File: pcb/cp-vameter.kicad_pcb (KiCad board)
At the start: 2 copper layers, 100 x 100 mm, 28 parts, among them J1 Vin JST-PH2, J10 Vin Header*, J11 Vin JST-PH2, J12 Grove Ext. INA260, J13 Grove Display, J14 Grove Keypad, J15 Conn Display, J16 Conn Keypad, J2 Vin Header*, J3 Vin Barrel-Jack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

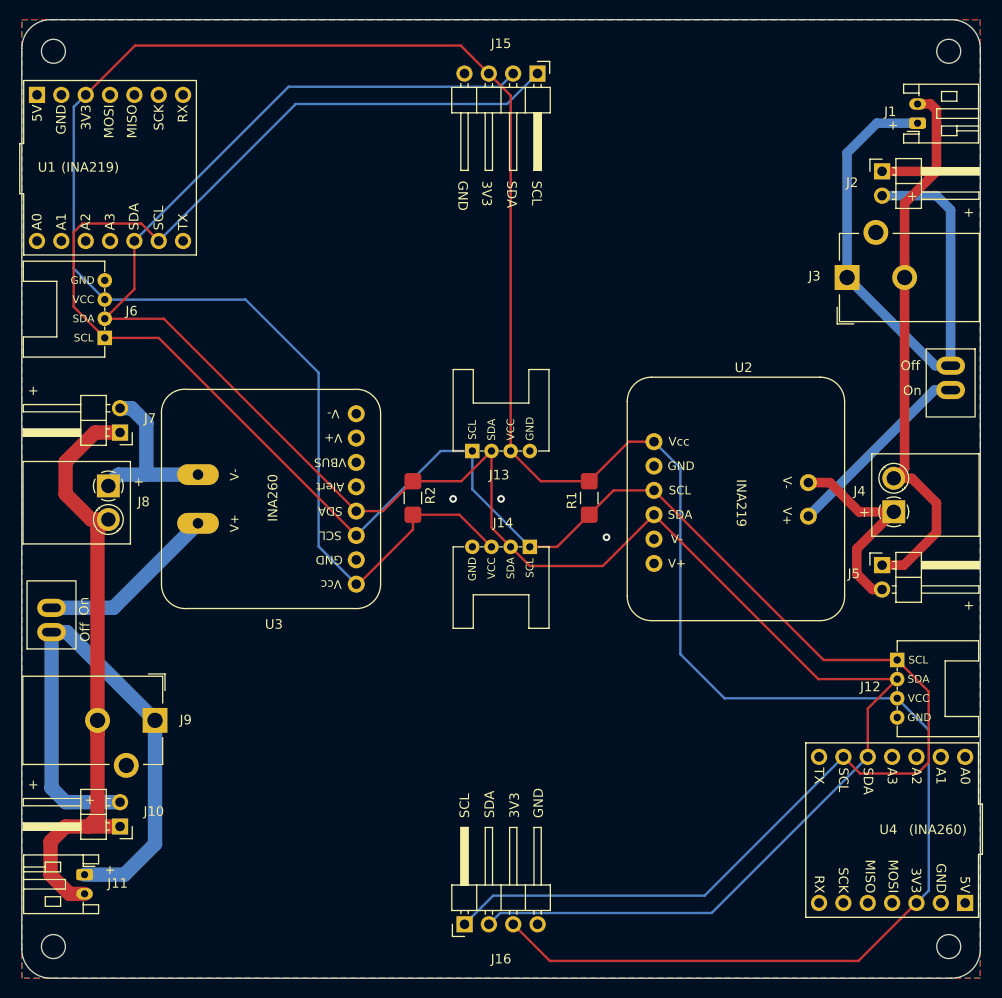
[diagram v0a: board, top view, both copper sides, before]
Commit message: replaced tht-footprint with smd-footprint for JST-connector in pcb
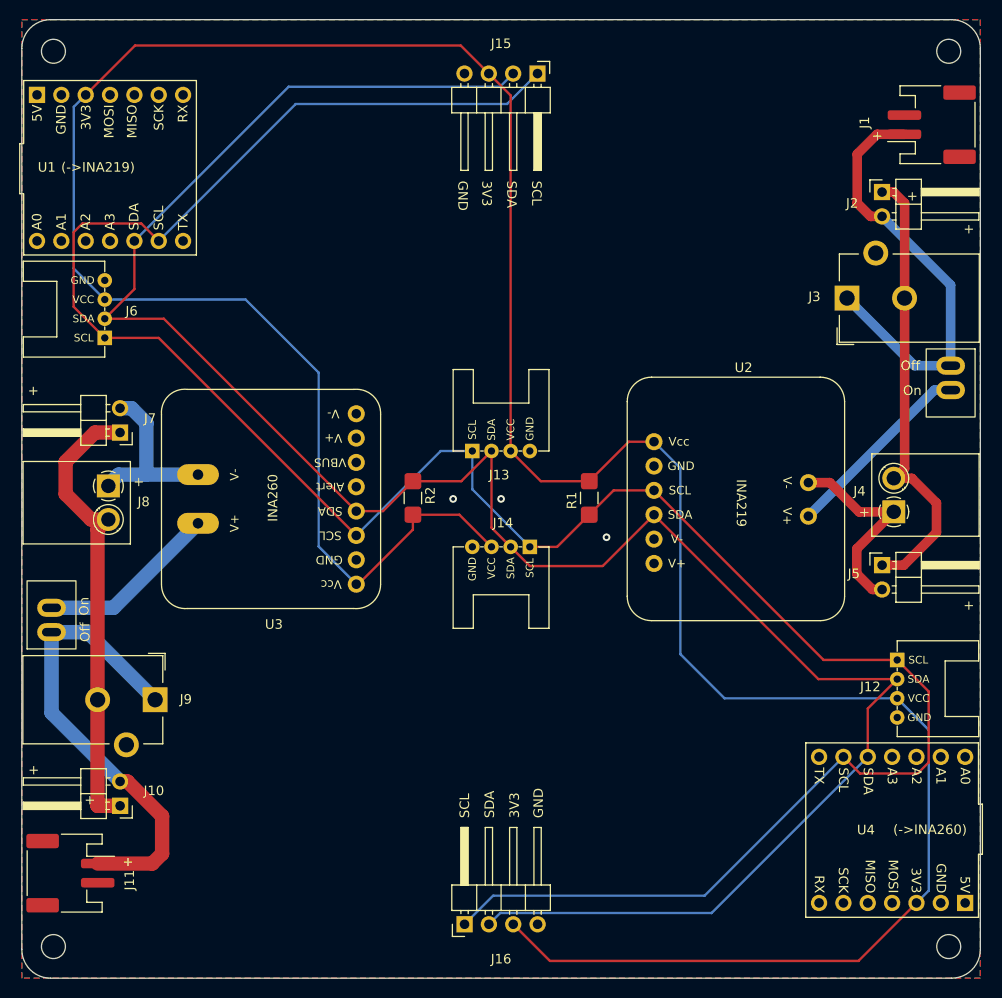
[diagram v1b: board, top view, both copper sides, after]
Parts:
- J1, J11: footprint Connector_JST:JST_PH_S2B-PH-K_1x02_P2.00mm_Horizontal -> Connector_JST:JST_PH_S2B-PH-SM4-TB_1x02-1MP_P2.00mm_Horizontal
- moved J10 2.16 mm to (-39.7, 32.0)
- moved J2 2.16 mm to (39.7, -32.0)
- moved J3 2.15 mm to (36.1, -20.9)
- moved J9 2.15 mm to (-36.1, 20.9)
- moved J1 1.49 mm to (44.9, -39.0)
- moved J11 1.49 mm to (-44.9, 39.0)
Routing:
- net GND: track 128.1 -> 95.9 mm
- net Net-(J1-Pad1): track 60.3 -> 46.3 mm
- net Net-(J10-Pad2): track 58.9 -> 49.2 mm
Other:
- board text added: "(->INA219)"
- board text added: "(->INA260)"
- board text added: "Rev: 1.1"
- board text removed: "(INA219)"
- board text removed: "(INA260)"
- board text removed: "Rev: 1.0"
